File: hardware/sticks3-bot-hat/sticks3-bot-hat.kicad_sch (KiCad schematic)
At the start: 23 parts, among them J1 HAT2_StickS3, J10 COLOR_B, J11 DC_6V_5525, J2 SERVO_A, J3 SERVO_B, J4 HEAD_PAN, J5 HEAD_TILT, J6 ENC_A, J7 ENC_B, J8 COLOR_A, U1 AP63205

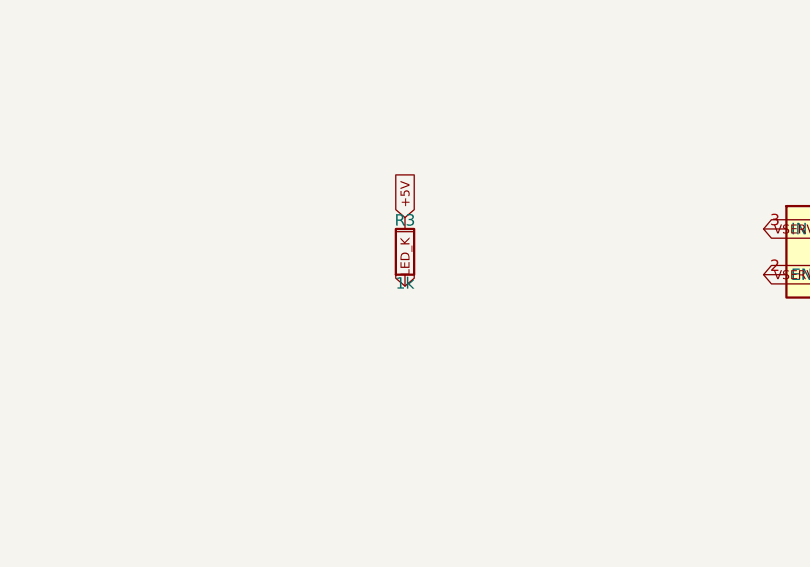
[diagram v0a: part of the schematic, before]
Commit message: Bot HAT: dim power LED (R3 22k), M3 mounting holes, dockerised fab export
- R3 1k -> 22k (~0.14 mA): the 1k LED on the first JLCPCB batch was far
  too bright for a power indicator. BOM/LCSC updated (C4190).
- Mounting holes H1-H4 changed in place from MountingHole_2.7mm_M2.5 to
  MountingHole_3.2mm_M3, same centres; GND zones refilled. The M3 head
  courtyard grazes J1/J2 by <0.25 mm (DRC warning) - use <=5.5 mm heads.
- export.sh: falls back to the kicad/kicad:10.0 docker image when
  kicad-cli isn't installed, runs DRC/ERC, exports the schematic PDF,
  and no longer deletes the hand-maintained cpl-jlcpcb-corrected.csv.
- Regenerated gerbers, drill, positions, BOM, schematic PDF, reports.
- .gitignore .venv/
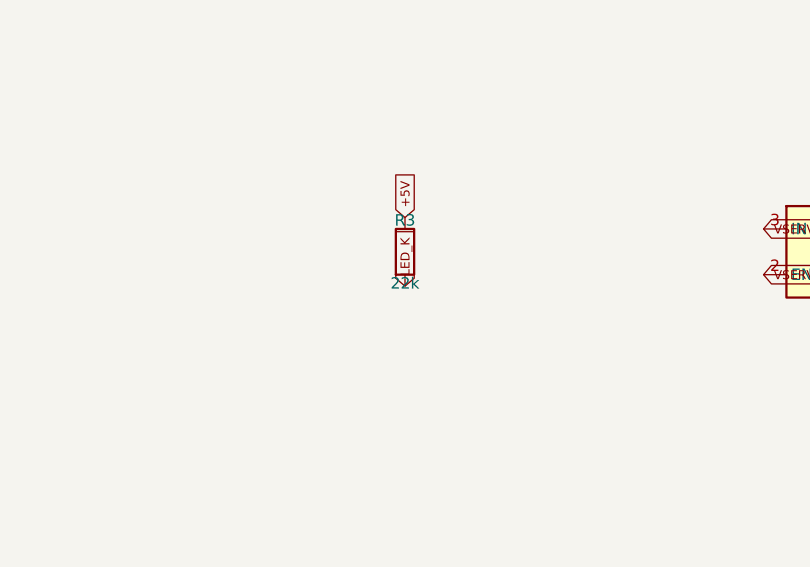
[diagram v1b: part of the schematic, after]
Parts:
- H1, H2, H3, H4: footprint MountingHole:MountingHole_2.7mm_M2.5 -> MountingHole:MountingHole_3.2mm_M3
- R3: value 1k -> 22k
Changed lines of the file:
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@@
     (property "Value" "M3" (at 40.0 88.5 0)
       (effects (font (size 1.27 1.27))))
-    (property "Footprint" "MountingHole:MountingHole_2.7mm_M2.5" (at 40.0 85.0 0)
+    (property "Footprint" "MountingHole:MountingHole_3.2mm_M3" (at 40.0 85.0 0)
       (effects (font (size 1.27 1.27)) (hide yes)))
     (instances
@@
     (property "Value" "M3" (at 90.0 88.5 0)
       (effects (font (size 1.27 1.27))))
-    (property "Footprint" "MountingHole:MountingHole_2.7mm_M2.5" (at 90.0 85.0 0)
+    (property "Footprint" "MountingHole:MountingHole_3.2mm_M3" (at 90.0 85.0 0)
       (effects (font (size 1.27 1.27)) (hide yes)))
     (instances
@@
     (property "Value" "M3" (at 140.0 88.5 0)
       (effects (font (size 1.27 1.27))))
-    (property "Footprint" "MountingHole:MountingHole_2.7mm_M2.5" (at 140.0 85.0 0)
+    (property "Footprint" "MountingHole:MountingHole_3.2mm_M3" (at 140.0 85.0 0)
       (effects (font (size 1.27 1.27)) (hide yes)))
     (instances
@@
     (property "Value" "M3" (at 190.0 88.5 0)
       (effects (font (size 1.27 1.27))))
-    (property "Footprint" "MountingHole:MountingHole_2.7mm_M2.5" (at 190.0 85.0 0)
+    (property "Footprint" "MountingHole:MountingHole_3.2mm_M3" (at 190.0 85.0 0)
       (effects (font (size 1.27 1.27)) (hide yes)))
     (instances
@@
     (property "Reference" "R3" (at 190.0 171.5 0)
       (effects (font (size 1.27 1.27))))
-    (property "Value" "1k" (at 190.0 178.5 0)
+    (property "Value" "22k" (at 190.0 178.5 0)
       (effects (font (size 1.27 1.27))))
     (property "Footprint" "Resistor_SMD:R_0603_1608Metric" (at 190.0 175.0 0)

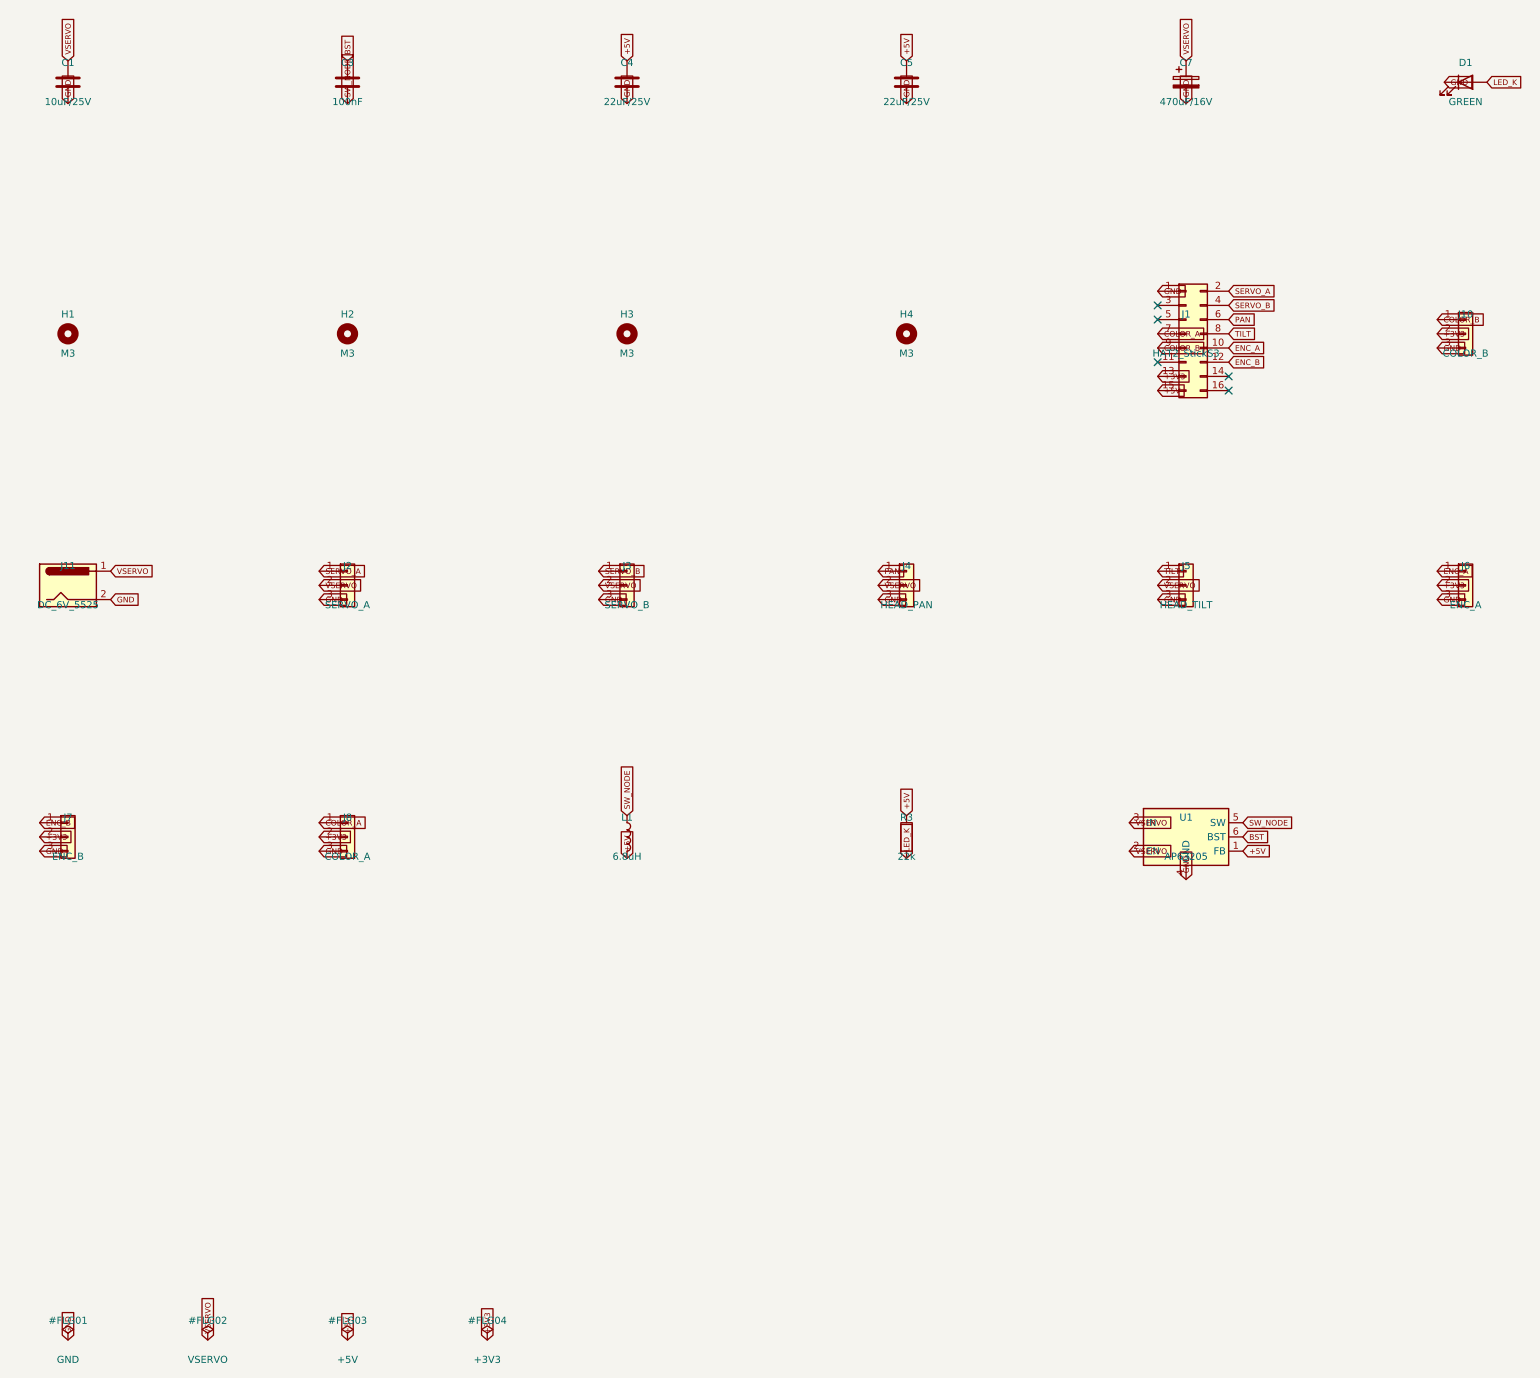
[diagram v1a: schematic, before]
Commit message: Bot HAT v4: LM393-order sensor headers, HC-SR04 DIST port, distance_sensor SDK
Board (hardware/sticks3-bot-hat, edited in place via gen/tools/rework_v4.py
so the hand routing survives):
- ENC A/B headers reordered to V G D0 and COLOR to V G - A0 (1x4) so the
  LM393 encoder / TCRT5000 modules connect with a straight Dupont cable.
- COLOR B replaced by DIST: 1x4 (5V TRIG ECHO GND) matching the HC-SR04,
  fed from the buck's 5 V; ECHO through a new 1k/2k divider (R4/R5) so the
  5 V pulse reaches G8 at 3.3 V; TRIG on the previously free G2.
- Power LED moved beside DIST. Schematic regenerated from design.py.
- DRC/ERC clean except the two known M3 courtyard warnings. Regenerated
  gerbers, drill, positions, BOM, JLC-corrected CPL (R3/D1/J10 moved,
  R4/R5 added), schematic PDF and renders (new gen/render.sh).
- gen_sch.py / export.sh / render.sh work with the kicad docker image.

Software:
- examples/sdk_distance_sensor.py: SPIKE-style distance(port) in mm
  (-1 out of range) plus distance_cm(); sdk_config gains
  DISTANCE_SENSOR_PINS, StickS3 color sensor is now port C on G1.
- Simulator: gears/minibot/distance_sensor.py on a forward UltrasonicSensor
  (in3, port D) added to robots/minibot.json; registered in skulpt.js.
- Scratch: "distance sensor (cm)" block; example.js lists the new SDK file.
- Docs: HAT README (connectors, GPIO map, ordering notes), CLAUDE.md,
  gears/README.md.
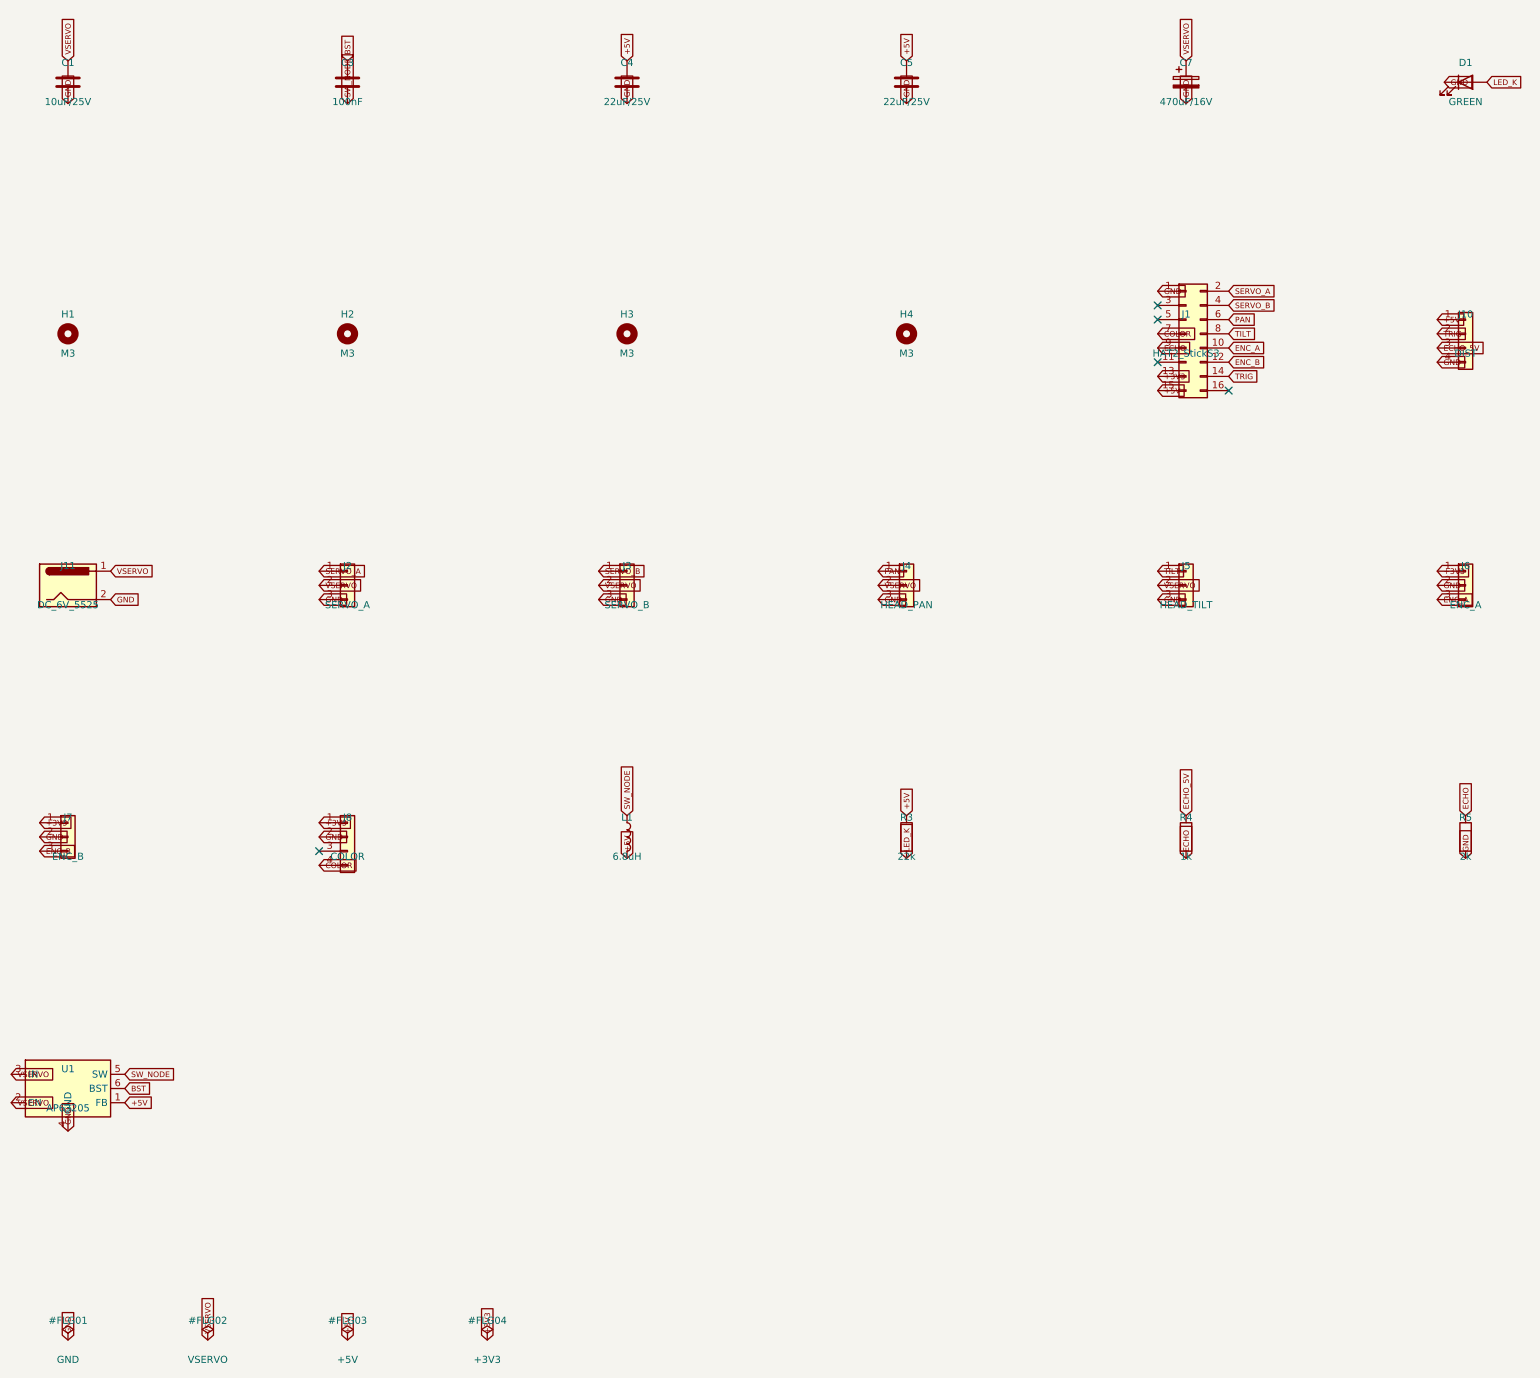
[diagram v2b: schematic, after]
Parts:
- removed J10: COLOR_B, Connector_PinHeader_2.54mm:PinHeader_1x03_P2.54mm_Vertical, symbol Connector_Generic:Conn_01x03
- removed J8: COLOR_A, Connector_PinHeader_2.54mm:PinHeader_1x03_P2.54mm_Vertical, symbol Connector_Generic:Conn_01x03
- added J10: DIST, Connector_PinHeader_2.54mm:PinHeader_1x04_P2.54mm_Vertical, symbol Connector_Generic:Conn_01x04
- added J8: COLOR, Connector_PinHeader_2.54mm:PinHeader_1x04_P2.54mm_Vertical, symbol Connector_Generic:Conn_01x04
- added R4: 1k, Resistor_SMD:R_0603_1608Metric, symbol Device:R
- added R5: 2k, Resistor_SMD:R_0603_1608Metric, symbol Device:R
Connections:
- net +3V3: now also J6.1 (Pin_1), J7.1 (Pin_1), J8.1 (Pin_1); no longer J6.2 (Pin_2), J7.2 (Pin_2)
- net +5V: now also J10.1 (Pin_1)
- net ENC_A: now also J6.3 (Pin_3); no longer J6.1 (Pin_1)
- net ENC_B: now also J7.3 (Pin_3); no longer J7.1 (Pin_1)
- net GND: now also J6.2 (Pin_2), J7.2 (Pin_2), J10.4 (Pin_4), J8.2 (Pin_2), R5.2; no longer J6.3 (Pin_3), J7.3 (Pin_3)
- net TRIG: now reaches J1.14 (Pin_14)
- net TRIG: now also J10.2 (Pin_2)
- net COLOR_A renamed COLOR
- net COLOR: now also J8.4 (Pin_4)
- net COLOR_B renamed ECHO
- net ECHO: now also R4.2, R5.1
- new net ECHO_5V: J10.3 (Pin_3), R4.1

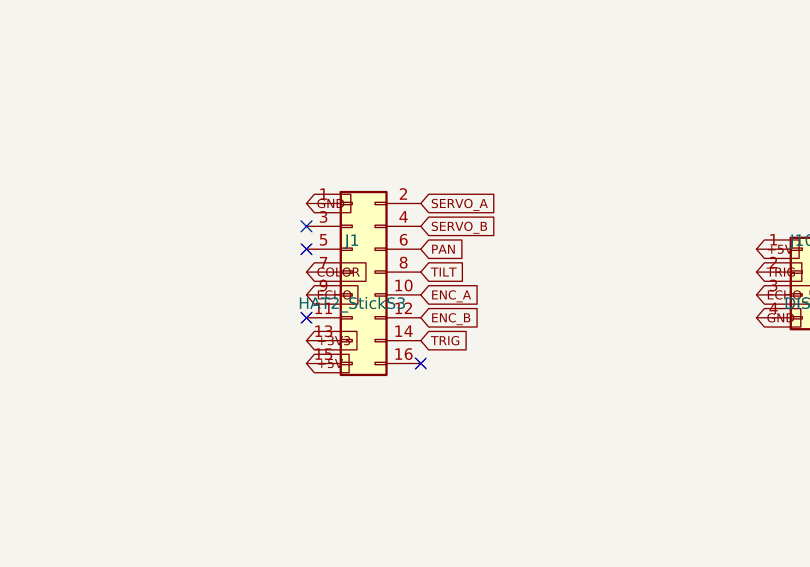
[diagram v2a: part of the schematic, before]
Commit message: Bot HAT v5: swap the J1 header rows (StickS3 power row is the lower pins)
Bring-up of the v3 board showed the StickS3, screen up, puts its power row
(GND EXT_5V BOOT G1 G8 BAT 3V3 5V_IN) on the header's lower pins and the
GPIO row on the upper pins; design.py had them the other way round (copied
from M5Stack's table, whose numbering starts on the power row). Columns
were right. Every other part of the board checked out on hardware with an
11-wire Dupont harness swapping the rows: buck 5 V, servo rail, all four
servo headers, both encoders and the reflection sensor.

- design.py: J1 nets moved to the other row in each column; comment records
  the measured socket layout.
- kicad_pcb: gen/tools/rework_v5_j1rows.py (text edit, no pcbnew) drops the
  30 segments / 3 vias fanning out to J1, adds the re-terminated routes
  (35 segments / 3 vias), renets J1 and strips the stale zone fills.
  Nothing else on the board moved. Same-layer clearance checked >= 0.2 mm.
- kicad_sch: J1 pin labels / no-connects moved to match.
- README: header-row explanation, field fix for v3/v4 boards, corrected
  first-article checks, and the KiCad steps still to run on the Mac
  (refill zones, DRC, export.sh, render.sh).
- export.sh refills zones before export (KiCad bundle python or docker);
  stale v4 gerbers removed from fab/ so they cannot be ordered.
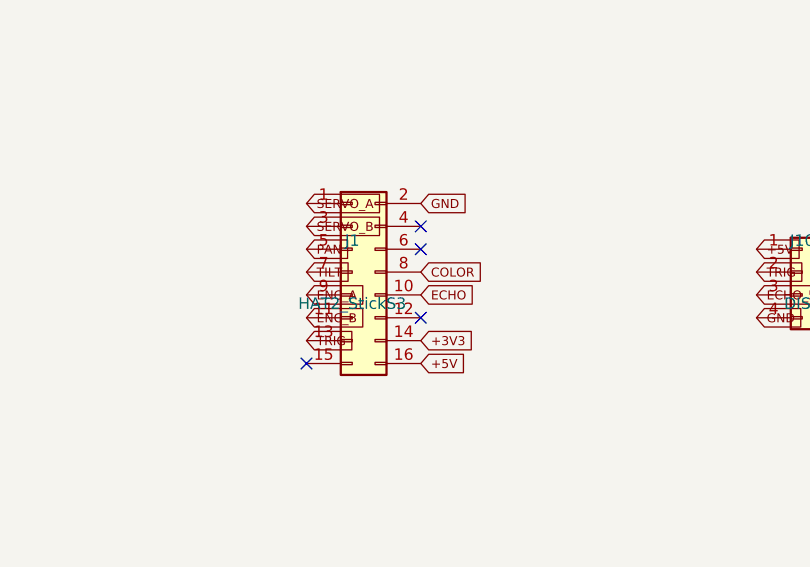
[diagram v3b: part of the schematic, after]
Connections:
- net +3V3: now also J1.14 (Pin_14); no longer J1.13 (Pin_13)
- net +5V: now also J1.16 (Pin_16); no longer J1.15 (Pin_15)
- net COLOR: now also J1.8 (Pin_8); no longer J1.7 (Pin_7)
- net ECHO: now also J1.10 (Pin_10); no longer J1.9 (Pin_9)
- net ENC_A: now also J1.9 (Pin_9); no longer J1.10 (Pin_10)
- net ENC_B: now also J1.11 (Pin_11); no longer J1.12 (Pin_12)
- net GND: now also J1.2 (Pin_2); no longer J1.1 (Pin_1)
- net PAN: now also J1.5 (Pin_5); no longer J1.6 (Pin_6)
- net SERVO_A: now also J1.1 (Pin_1); no longer J1.2 (Pin_2)
- net SERVO_B: now also J1.3 (Pin_3); no longer J1.4 (Pin_4)
- net TILT: now also J1.7 (Pin_7); no longer J1.8 (Pin_8)
- net TRIG: now also J1.13 (Pin_13); no longer J1.14 (Pin_14)
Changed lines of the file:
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@@
         (path "/76cba402-eb9b-48ec-82b7-eefdaa9b8bf7" (reference "J1") (unit 1))))
   )
-  (global_label "GND"
+  (global_label "SERVO_A"
     (shape input)
     (at 234.92 77.38 180)
     (effects (font (size 1.0 1.0)) (justify left))
   )
-  (global_label "SERVO_A"
+  (global_label "GND"
     (shape input)
     (at 247.62 77.38 0)
     (effects (font (size 1.0 1.0)) (justify left))
   )
-  (no_connect (at 234.92 79.92))
   (global_label "SERVO_B"
     (shape input)
-    (at 247.62 79.92 0)
+    (at 234.92 79.92 180)
     (effects (font (size 1.0 1.0)) (justify left))
   )
-  (no_connect (at 234.92 82.46))
+  (no_connect (at 247.62 79.92))
   (global_label "PAN"
     (shape input)
-    (at 247.62 82.46 0)
+    (at 234.92 82.46 180)
+    (effects (font (size 1.0 1.0)) (justify left))
+  )
+  (no_connect (at 247.62 82.46))
+  (global_label "TILT"
+    (shape input)
+    (at 234.92 85.0 180)
     (effects (font (size 1.0 1.0)) (justify left))
   )
   (global_label "COLOR"
     (shape input)
-    (at 234.92 85.0 180)
+    (at 247.62 85.0 0)
     (effects (font (size 1.0 1.0)) (justify left))
   )
-  (global_label "TILT"
+  (global_label "ENC_A"
     (shape input)
-    (at 247.62 85.0 0)
+    (at 234.92 87.54 180)
     (effects (font (size 1.0 1.0)) (justify left))
   )
   (global_label "ECHO"
     (shape input)
-    (at 234.92 87.54 180)
-    (effects (font (size 1.0 1.0)) (justify left))
-  )
-  (global_label "ENC_A"
-    (shape input)
     (at 247.62 87.54 0)
     (effects (font (size 1.0 1.0)) (justify left))
   )
-  (no_connect (at 234.92 90.08))
   (global_label "ENC_B"
     (shape input)
-    (at 247.62 90.08 0)
+    (at 234.92 90.08 180)
+    (effects (font (size 1.0 1.0)) (justify left))
+  )
+  (no_connect (at 247.62 90.08))
+  (global_label "TRIG"
+    (shape input)
+    (at 234.92 92.62 180)
     (effects (font (size 1.0 1.0)) (justify left))
   )
   (global_label "+3V3"
     (shape input)
-    (at 234.92 92.62 180)
-    (effects (font (size 1.0 1.0)) (justify left))
-  )
-  (global_label "TRIG"
-    (shape input)
     (at 247.62 92.62 0)
     (effects (font (size 1.0 1.0)) (justify left))
   )
+  (no_connect (at 234.92 95.16))
   (global_label "+5V"
     (shape input)
-    (at 234.92 95.16 180)
+    (at 247.62 95.16 0)
     (effects (font (size 1.0 1.0)) (justify left))
   )
-  (no_connect (at 247.62 95.16))
   (symbol
     (lib_id "Connector_Generic:Conn_01x04")
